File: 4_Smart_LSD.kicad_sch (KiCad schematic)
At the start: 14 parts, among them U15 VNLD5090TR-E, U20 VNLD5090TR-E

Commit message: All the diodes, and other layout work
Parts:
- added D33, D34, D35, D36, D37, D38, D39, D40: BAT54S, Package_TO_SOT_SMD:SOT-523, symbol Diode:BAT54S
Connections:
- net GND: now also D33.1 (A), D34.1 (A), D35.1 (A), D36.1 (A), D37.1 (A), D38.1 (A), D39.1 (A), D40.1 (A)
- net In1: now also D33.3 (COM)
- net In2: now also D35.3 (COM)
- net In3: now also D37.3 (COM)
- net In4: now also D39.3 (COM)
- net Status1: now also D34.3 (COM)
- net Status2: now also D36.3 (COM)
- net Status3: now also D38.3 (COM)
- net Status4: now also D40.3 (COM)
- net Logic_V renamed V_{logic}
- net V_{logic}: now also D33.2 (K), D34.2 (K), D35.2 (K), D36.2 (K), D37.2 (K), D38.2 (K), D39.2 (K), D40.2 (K)

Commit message: Finalised RS485 Circuit, Layout improvemnts, mounting holes, silkscreen...
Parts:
- U15, U20: LCSC (none) -> C222209
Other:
- company: (none) -> eChook
- title: (none) -> BMS Comms Master Board
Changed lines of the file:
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@@
 	(generator_version "9.0")
 	(paper "A4")
+	(title_block
+		(title "BMS Comms Master Board")
+		(date "2025-05-21")
+		(rev "0.1")
+		(company "eChook")
+	)
 	(junction
 		(at 238.76 77.47)
@@
 			)
 		)
+		(property "LCSC" "C222209"
+			(at 135.89 113.03 0)
+			(effects
+				(font
+					(size 1.27 1.27)
+				)
+			)
+		)
 		(pin "4"
 		)
@@
 			)
 		)
+		(property "LCSC" "C222209"
+			(at 135.89 74.93 0)
+			(effects
+				(font
+					(size 1.27 1.27)
+				)
+			)
+		)

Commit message: Added UART Buffer for Aux Connector Serial
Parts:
- R42, R44, R46, R48, R49, R50, R51, R52: now left out of the parts list
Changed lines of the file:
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@@
 		(unit 1)
 		(exclude_from_sim no)
-		(in_bom yes)
-		(on_board yes)
+		(in_bom no)
+		(on_board no)
 		(dnp no)
 		(property "Reference" "R51"
@@
 		(unit 1)
 		(exclude_from_sim no)
-		(in_bom yes)
-		(on_board yes)
+		(in_bom no)
+		(on_board no)
 		(dnp no)
 		(property "Reference" "R46"
@@
 		(unit 1)
 		(exclude_from_sim no)
-		(in_bom yes)
-		(on_board yes)
+		(in_bom no)
+		(on_board no)
 		(dnp no)
 		(property "Reference" "R48"
@@
 		(unit 1)
 		(exclude_from_sim no)
-		(in_bom yes)
-		(on_board yes)
+		(in_bom no)
+		(on_board no)
 		(dnp no)
 		(property "Reference" "R52"
@@
 		(unit 1)
 		(exclude_from_sim no)
-		(in_bom yes)
-		(on_board yes)
+		(in_bom no)
+		(on_board no)
 		(dnp no)
 		(property "Reference" "R42"
@@
 		(unit 1)
 		(exclude_from_sim no)
-		(in_bom yes)
-		(on_board yes)
+		(in_bom no)
+		(on_board no)
 		(dnp no)
 		(property "Reference" "R49"
@@
 		(unit 1)
 		(exclude_from_sim no)
-		(in_bom yes)
-		(on_board yes)
+		(in_bom no)
+		(on_board no)
 		(dnp no)
 		(property "Reference" "R50"
@@
 		(unit 1)
 		(exclude_from_sim no)
-		(in_bom yes)
-		(on_board yes)
+		(in_bom no)
+		(on_board no)
 		(dnp no)
 		(property "Reference" "R44"

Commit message: PCB Improvements - VIAS/Pours UNFINISHED
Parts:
- D34, D36, D38, D40: now not fitted; now left out of the parts list
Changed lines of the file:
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@@
 		(unit 1)
 		(exclude_from_sim no)
-		(in_bom yes)
-		(on_board yes)
-		(dnp no)
+		(in_bom no)
+		(on_board no)
+		(dnp yes)
 		(fields_autoplaced yes)
 		(property "Reference" "D34"
@@
 		(unit 1)
 		(exclude_from_sim no)
-		(in_bom yes)
-		(on_board yes)
-		(dnp no)
+		(in_bom no)
+		(on_board no)
+		(dnp yes)
 		(fields_autoplaced yes)
 		(property "Reference" "D36"
@@
 		(unit 1)
 		(exclude_from_sim no)
-		(in_bom yes)
-		(on_board yes)
-		(dnp no)
+		(in_bom no)
+		(on_board no)
+		(dnp yes)
 		(fields_autoplaced yes)
 		(property "Reference" "D38"
@@
 		(unit 1)
 		(exclude_from_sim no)
-		(in_bom yes)
-		(on_board yes)
-		(dnp no)
+		(in_bom no)
+		(on_board no)
+		(dnp yes)
 		(property "Reference" "D40"
 			(at 252.73 33.0199 90)

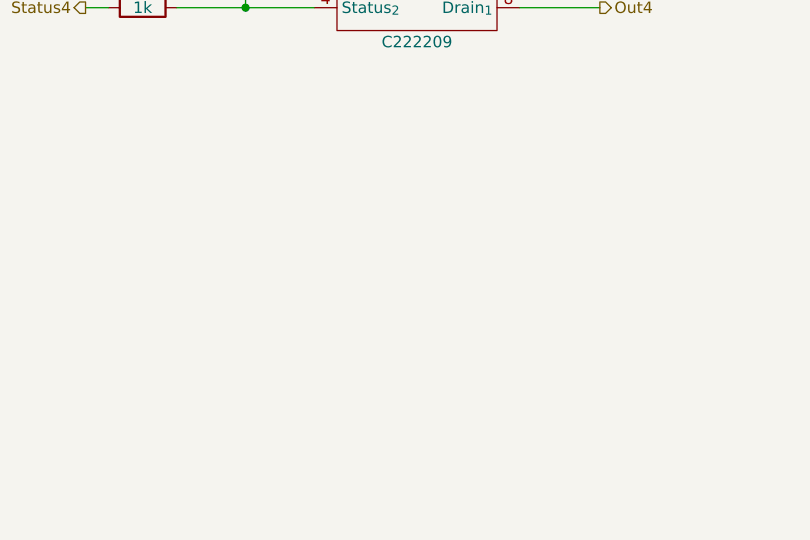
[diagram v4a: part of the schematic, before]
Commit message: Added pulldown safety resistors, layout improvements
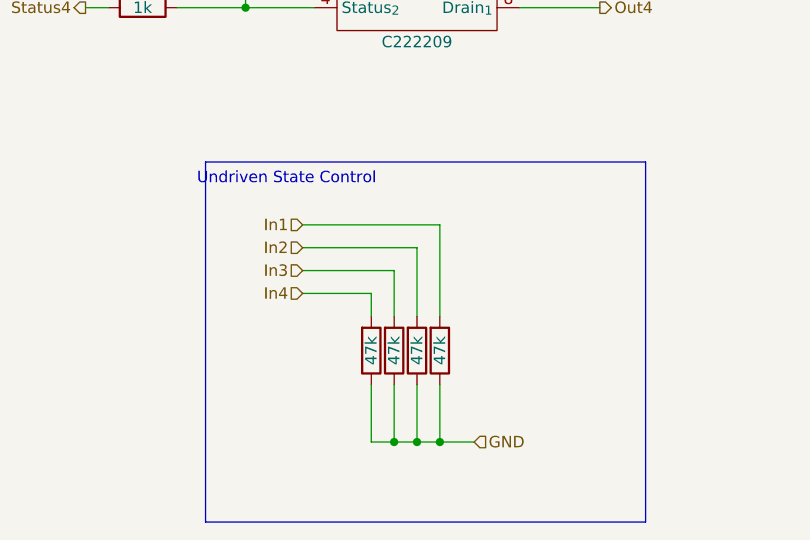
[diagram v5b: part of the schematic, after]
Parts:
- added R87, R88, R89, R90: 47k, Resistor_SMD:R_0603_1608Metric, symbol Device:R
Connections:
- net GND: now also R87.1, R88.1, R89.1, R90.1
- net In1: now also R90.2
- net In2: now also R89.2
- net In3: now also R88.2
- net In4: now also R87.2
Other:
- note added: "Undriven State Control"
